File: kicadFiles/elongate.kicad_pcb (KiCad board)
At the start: 2 copper layers, 294 x 82 mm, 141 parts, among them J1 USB_B_Mini, SW1 MXSwitch, SW10 MXSwitch, SW11 MXSwitch, SW12 MXSwitch, SW13 MXSwitch, SW14 MXSwitch, SW15 MXSwitch, SW16 MXSwitch, SW17 MXSwitch, SW18 MXSwitch, SW19 MXSwitch, SW2 MXSwitch, SW20 MXSwitch, SW21 MXSwitch, SW22 MXSwitch, SW23 MXSwitch, SW24 MXSwitch, SW25 MXSwitch, SW26 MXSwitch, SW27 MXSwitch, SW28 MXSwitch, SW29 MXSwitch, SW3 MXSwitch, SW30 MXSwitch, SW31 MXSwitch, SW32 MXSwitch, SW33 MXSwitch, SW34 MXSwitch, SW35 MXSwitch, SW36 MXSwitch, SW37 MXSwitch, SW38 MXSwitch, SW39 MXSwitch, SW4 MXSwitch, SW40 MXSwitch, SW41 MXSwitch, SW42 MXSwitch, SW43 MXSwitch, SW44 MXSwitch, SW45 MXSwitch, SW46 MXSwitch, SW47 MXSwitch, SW48 MXSwitch, SW49 MXSwitch, SW5 MXSwitch, SW50 MXSwitch, SW51 MXSwitch, SW52 MXSwitch, SW53 MXSwitch, SW54 MXSwitch, SW6 MXSwitch, SW7 MXSwitch, SW8 MXSwitch, SW9 MXSwitch, U2 USBLC6-2SC6, U3 ATMEGA32U4, X1 16MHz

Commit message: Started mirroring PCB
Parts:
- L2: moved to B.Cu
- X1: footprint acheron_Components:Crystal_SMD_5032-4Pin-HandSolder -> acheron_Components:Crystal_SMD_5032-4Pin
- moved SW1 276.2 mm to (419.8, 63.5)
- moved SW15 276.2 mm to (143.5, 63.5)
- moved SW29 276.2 mm to (143.5, 82.6)
- moved SW43 276.2 mm to (143.5, 101.6)
- moved SW54 276.2 mm to (143.5, 120.7)
- moved D16 271.5 mm to (426.9, 82.6)
- moved D44 271.5 mm to (426.9, 120.7)
- moved SW16 271.5 mm to (417.4, 82.6)
- moved SW44 271.5 mm to (417.4, 120.7)
- moved D43 266.9 mm to (153.1, 101.6), turned to 90 degrees
- moved D54 266.9 mm to (153.1, 120.7), turned to 90 degrees
- moved D29 266.8 mm to (153.1, 82.6), turned to 90 degrees
- moved D15 266.8 mm to (153.1, 63.5), turned to 90 degrees
- moved SW30 261.9 mm to (412.6, 101.6)
- moved D30 259.6 mm to (422.1, 98.1), turned to 270 degrees
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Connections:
- CUSB1 pad 1: 5V -> VBUS
- F1 pad 2: Net-(F1-Pad2) -> VBUS
- J1 pad 1: Net-(F1-Pad2) -> VBUS
- U2 pad 5: 5V -> VBUS
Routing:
- net Col1: track 347.0 -> 116.6 mm
- net Col13: track 126.1 -> 309.8 mm
- net Col11: track 139.3 -> 313.8 mm
- net Col4: track 215.4 -> 41.5 mm
- net Col2: track 298.5 -> 151.9 mm
- net Col10: track 158.9 -> 298.0 mm
- net Row1: track 340.7 -> 443.0 mm
- net Col8: track 197.8 -> 278.4 mm
- net Col3: track 291.4 -> 214.5 mm
- net Col6: track 184.3 -> 114.8 mm
- net Col7: track 163.8 -> 94.8 mm
- net Row2: track 347.0 -> 411.3 mm
- net Col9: track 126.7 -> 78.2 mm
- net Col15: track 116.3 -> 79.4 mm
- net Row4: track 359.3 -> 331.5 mm
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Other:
- outline, holes or cut-outs redrawn
- board text removed: "ATMEGA32U4"

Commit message: Breakout pins, refresh gerbers
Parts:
- RHWB1: value 1k -> 10k
- X1: footprint acheron_Components:Crystal_SMD_5032-4Pin -> acheron_Components:Crystal_SMD_5032-4Pin_5.0x3.2mm
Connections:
- U3 pad 12: Col4 -> Net-(U3-Pad12)
- U3 pad 18: Net-(U3-Pad18) -> Row3
- U3 pad 19: Col6 -> Col15
- U3 pad 20: Col7 -> Col14
- U3 pad 21: Col9 -> Col13
- U3 pad 22: Col12 -> Row4
- U3 pad 25: Col1 -> Col12
- U3 pad 26: Col2 -> Col11
- U3 pad 27: Col3 -> Col10
- U3 pad 28: Col5 -> Col8
- U3 pad 29: Col8 -> Col5
- U3 pad 30: Col10 -> Col3
- U3 pad 31: Col11 -> Col2
- U3 pad 32: Col13 -> Col1
- U3 pad 36: Row4 -> Col9
- U3 pad 37: Row3 -> Col7
- U3 pad 38: Col14 -> Col6
- U3 pad 39: Col15 -> Col4
- U3 pad 40: Row2 -> Net-(U3-Pad40)
- U3 pad 41: Row1 -> Net-(U3-Pad41)
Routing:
- net Col13: track 309.8 -> 103.3 mm
- net Col1: track 116.6 -> 312.1 mm
- net Col11: track 313.8 -> 121.6 mm
- net Col4: track 41.5 -> 203.8 mm
- net Col2: track 151.9 -> 304.2 mm
- net Col10: track 298.0 -> 146.3 mm
- net Col3: track 214.5 -> 308.3 mm
- net Col8: track 278.4 -> 188.2 mm
- net Col15: track 79.4 -> 138.9 mm
- net Row3: track 362.0 -> 413.4 mm
- net Col7: track 94.8 -> 145.9 mm
- net Col6: track 114.8 -> 165.5 mm
- net Col14: track 79.4 -> 116.2 mm
- net Col9: track 78.2 -> 110.7 mm
- net Row4: track 331.5 -> 355.9 mm
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
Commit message: Breakout pins, refresh gerbers
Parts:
- added J2: Conn_01x06_Female, acheron_Connectors:HEADER_6PIN, F.Cu at (143.5, 72.5)
- moved CU1 3.15 mm to (196.5, 75.7)
- moved CSH1 0.13 mm to (204.4, 57.7)
- moved D1 0.08 mm to (411.5, 63.5)
- moved D2 0.08 mm to (409.0, 63.5)
- moved D13 0.08 mm to (173.4, 63.5)
- moved D14 0.08 mm to (170.8, 63.5)
- moved D27 0.08 mm to (173.4, 82.6)
- moved D28 0.08 mm to (170.8, 82.6)
- moved D41 0.08 mm to (173.4, 101.6)
- moved D42 0.08 mm to (170.8, 101.6)
- moved RSH1 0.06 mm to (202.4, 57.7)
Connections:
- U3 pad 10: Net-(U3-Pad10) -> Pin10
- U3 pad 11: Net-(U3-Pad11) -> Pin11
- U3 pad 12: Net-(U3-Pad12) -> Pin12
- U3 pad 40: Net-(U3-Pad40) -> Row2
- U3 pad 41: Net-(U3-Pad41) -> Row1
- U3 pad 8: Net-(U3-Pad8) -> Pin8
- U3 pad 9: Net-(U3-Pad9) -> Pin9
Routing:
- net Pin12: track 0.00 -> 73.4 mm
- net Pin11: track 0.00 -> 70.6 mm
- net Pin10: track 0.00 -> 70.2 mm
- net Pin9: track 0.00 -> 69.4 mm
- net Pin8: track 0.00 -> 68.5 mm
- net Net-(CU1-Pad1): track 2.64 -> 6.23 mm
- net /RST: track 17.7 -> 20.3 mm
- net 5V: track 134.4 -> 131.9 mm, vias 8 -> 9
- net GND: vias 1 -> 2
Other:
- board text added: "GND"
- board text added: "PB0"
- board text added: "PB1"
- board text added: "PB2"
- board text added: "PB3"
- board text added: "PB7"

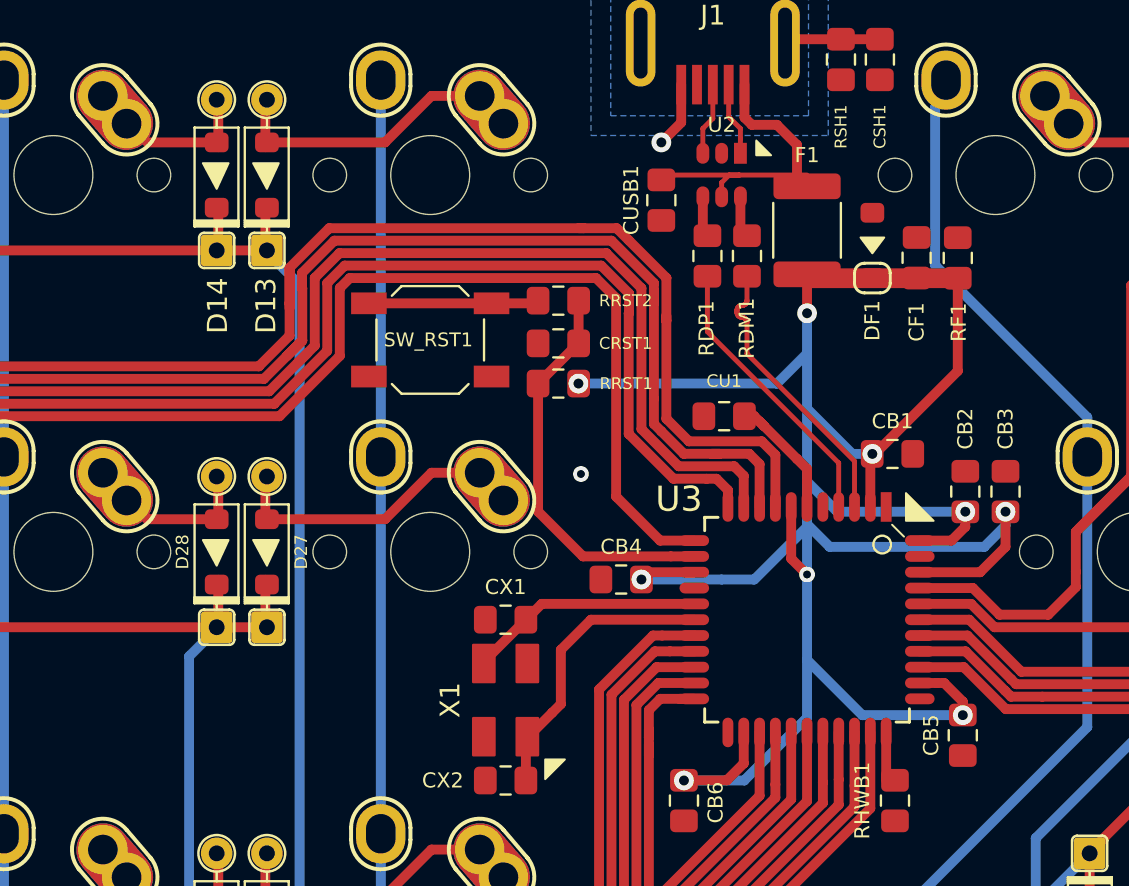
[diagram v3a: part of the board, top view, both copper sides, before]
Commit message: Fix pins 34/35, optimized VCC routing
- I dun goofed with the routing of pins 34 and 35, which are respectively VCC and GND, and they were routed the opposite way, which caused a short-circuit between VCC and GND, hindering be board bricked.

- There was a little optimization in the routing of the 5V net, specifically the trace going from the fuse. That trace was supposed to go trhough DF1, RF1 and CF1 and then to the MCU, when in reality the trace was coming directly from F1, precarizing the functionality of DF1, RF1 and CF1.

- A new schematic file was added to ./manuFiles/ folder

- Gerbers were refreshed
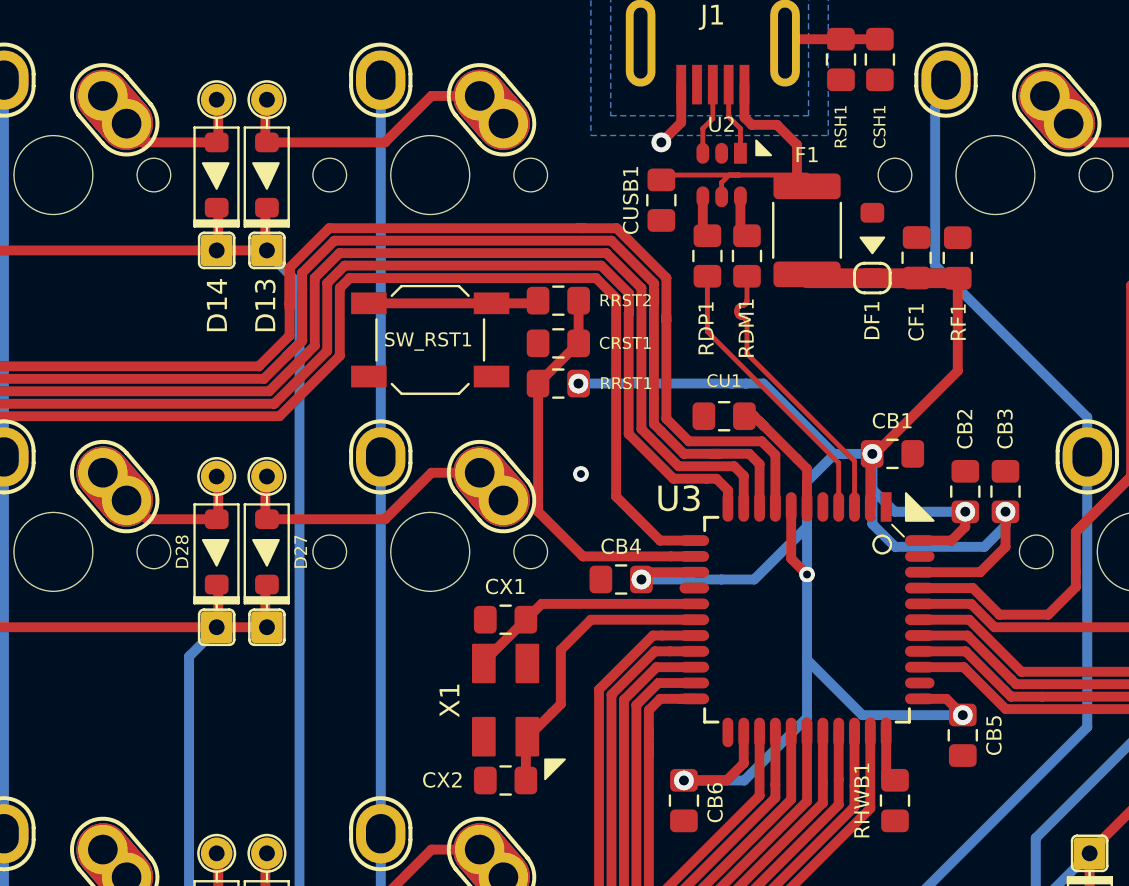
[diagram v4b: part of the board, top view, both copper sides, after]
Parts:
- RHWB1: value 10k -> 1k
- turned CB5 to 90 degrees
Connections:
- CB5 pad 1: 5V -> GND
- CB5 pad 2: GND -> 5V
- U3 pad 34: GND -> 5V
- U3 pad 35: 5V -> GND
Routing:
- net 5V: track 131.9 -> 120.3 mm, vias 9 -> 8
- net Net-(D14-Pad2): track 5.74 -> 7.34 mm

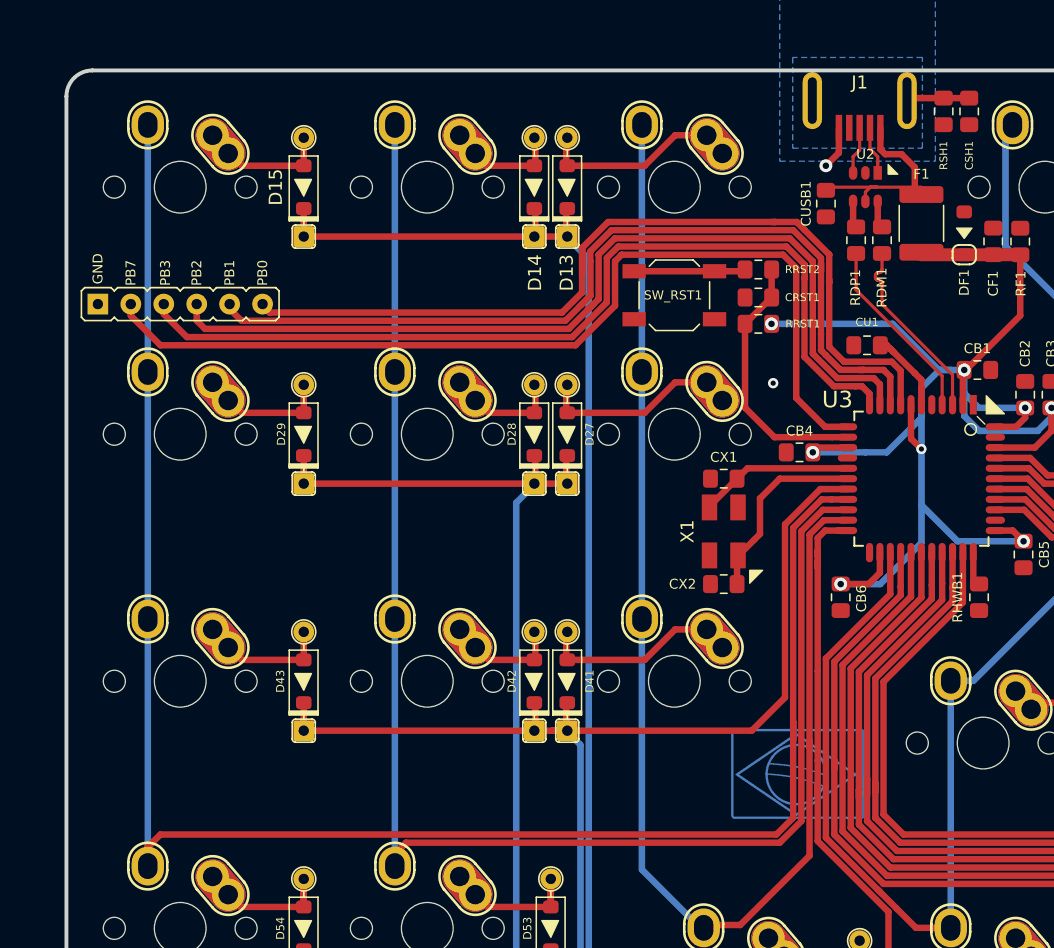
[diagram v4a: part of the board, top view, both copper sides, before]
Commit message: Expose ISP pins, rewire two cols
- The ISP pins (PB1, PB2, PB3, RST, GND, VCC) were exposed ("broken out") so that ISP is more easily done;

- Col 1 and col 2 were reassigned in the microcontroller for a better feeling
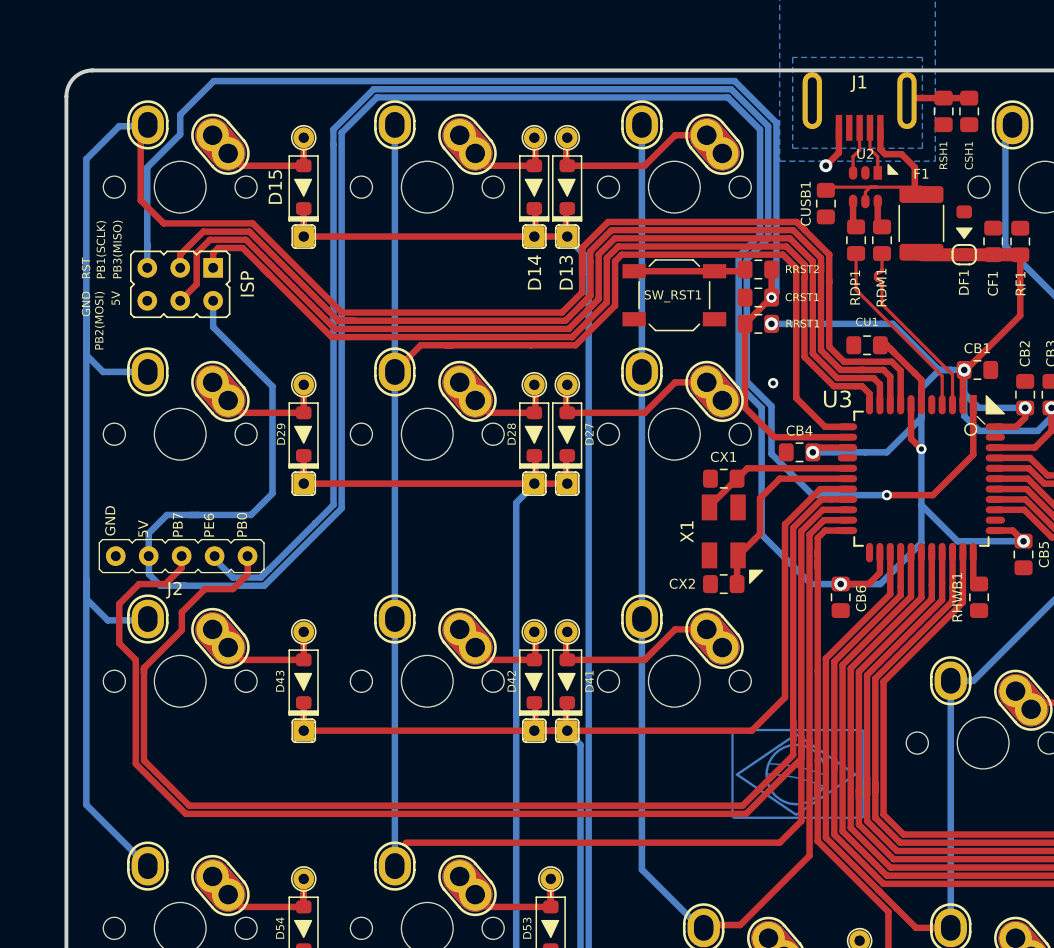
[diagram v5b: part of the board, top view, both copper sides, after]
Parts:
- added J3: Conn_01x06_Female, acheron_Connectors:HEADER_6PIN_HORIZONTAL, F.Cu at (143.5, 71.0)
- J2: footprint acheron_Connectors:HEADER_6PIN -> acheron_Connectors:HEADER_5PIN
- moved J2 20.1 mm to (138.6, 92.0)
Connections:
- net /RST renamed RST
- J2 pad 2: Pin12 -> 5V
- J2 pad 3: Pin11 -> PD2
- J2 pad 4: Pin10 -> PE6
- J2 pad 5: Pin9 -> PD1
- U3 pad 1: Net-(U3-Pad1) -> PE6
- U3 pad 10: Pin10 -> PB2
- U3 pad 11: Pin11 -> PB3
- U3 pad 12: Pin12 -> Col14
- U3 pad 19: Col15 -> PD1
- U3 pad 20: Col14 -> PD2
- U3 pad 8: Pin8 -> Col15
- U3 pad 9: Pin9 -> PB1
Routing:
- net 5V: track 120.3 -> 273.8 mm
- net PD2: track 0.00 -> 133.6 mm
- net PE6: track 0.00 -> 125.8 mm, vias 0 -> 1
- net PD1: track 0.00 -> 98.2 mm
- net PB1: track 0.00 -> 78.8 mm
- net PB2: track 0.00 -> 76.1 mm
- net RST: track 20.3 -> 95.9 mm, vias 0 -> 1
- net Pin12: track 73.4 -> 0.00 mm
- net Pin11: track 70.6 -> 0.00 mm
- net PB3: track 0.00 -> 70.2 mm
- net Pin10: track 70.2 -> 0.00 mm
- net Pin9: track 69.4 -> 0.00 mm
- net Pin8: track 68.5 -> 0.00 mm
- net Col15: track 138.9 -> 167.0 mm
- net Col14: track 116.2 -> 109.7 mm
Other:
- board text added: "5V"
- board text added: "ISP"
- board text added: "PB1(SCLK)"
- board text added: "PB2(MOSI)"
- board text added: "PB3(MISO)"
- board text added: "PE6"
- board text added: "RST"
- board text removed: "PB1"
- board text removed: "PB2"
- board text removed: "PB3"

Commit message: Add RGB WS2812 LEDs to schematic
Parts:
- added CRGB1: 10nF, Capacitor_SMD:C_0805_2012Metric_Pad1.15x1.40mm_HandSolder, F.Cu at (156.6, 108.4)
- added CRGB2: 10nF, Capacitor_SMD:C_0805_2012Metric_Pad1.15x1.40mm_HandSolder, F.Cu at (283.1, 110.6)
- added CRGB3: 10nF, Capacitor_SMD:C_0805_2012Metric_Pad1.15x1.40mm_HandSolder, F.Cu at (395.1, 110.8)
- added CRGB4: 10nF, Capacitor_SMD:C_0805_2012Metric_Pad1.15x1.40mm_HandSolder, F.Cu at (394.7, 72.5)
- added CRGB5: 10nF, Capacitor_SMD:C_0805_2012Metric_Pad1.15x1.40mm_HandSolder, F.Cu at (283.1, 72.5)
- added CRGB6: 10nF, Capacitor_SMD:C_0805_2012Metric_Pad1.15x1.40mm_HandSolder, F.Cu at (157.0, 70.1)
- added RGB1: WS2812B, acheron_Components:LED_WS2812B_5.0x5.0mm_P3.2mm, F.Cu at (162.6, 108.8)
- added RGB2: WS2812B, acheron_Components:LED_WS2812B_5.0x5.0mm_P3.2mm, F.Cu at (288.8, 111.2)
- added RGB3: WS2812B, acheron_Components:LED_WS2812B_5.0x5.0mm_P3.2mm, F.Cu at (400.7, 111.2)
- added RGB4: WS2812B, acheron_Components:LED_WS2812B_5.0x5.0mm_P3.2mm, F.Cu at (400.7, 73.0)
- added RGB5: WS2812B, acheron_Components:LED_WS2812B_5.0x5.0mm_P3.2mm, F.Cu at (288.8, 73.0)
- added RGB6: WS2812B, acheron_Components:LED_WS2812B_5.0x5.0mm_P3.2mm, F.Cu at (162.6, 70.7)
- J2: footprint acheron_Connectors:HEADER_5PIN -> acheron_Connectors:HEADER_4PIN
- moved L1 92.7 mm to (204.5, 112.9)
- moved D16 1.56 mm to (425.3, 82.6)
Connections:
- J2 pad 3: PD2 -> PE6
- J2 pad 4: PE6 -> PD1
- U3 pad 19: PD1 -> RGB_DIN
- U3 pad 20: PD2 -> PD1
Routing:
- net 5V: track 273.8 -> 681.6 mm, vias 8 -> 13
- net Net-(RGB5-Pad2): track 0.00 -> 239.7 mm, vias 0 -> 2
- net Net-(RGB1-Pad2): track 0.00 -> 186.0 mm, vias 0 -> 2
- net Net-(RGB2-Pad2): track 0.00 -> 174.6 mm
- net PD2: track 133.6 -> 0.00 mm
- net Net-(RGB4-Pad2): track 0.00 -> 108.2 mm
- net Net-(RGB3-Pad2): track 0.00 -> 87.1 mm
- net RGB_DIN: track 0.00 -> 45.9 mm
- net Col5: track 243.4 -> 253.0 mm
- net Row4: track 355.9 -> 361.7 mm
- net PE6: track 125.8 -> 129.5 mm
- net Row3: track 413.4 -> 416.2 mm
- net PD1: track 98.2 -> 100.7 mm
- net Row1: track 443.0 -> 444.5 mm
- net Col3: track 308.3 -> 309.4 mm
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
